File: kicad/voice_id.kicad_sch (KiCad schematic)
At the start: 23 parts, among them J1 Conn_01x08, J2 Audio Out (Speaker), J3 Reset, J4 Fan (5V 0.1A), J6 RV 10k, J7 Conn_01x04, SW1 PWR_SW, U2 LM7805_TO220, U3 Pico

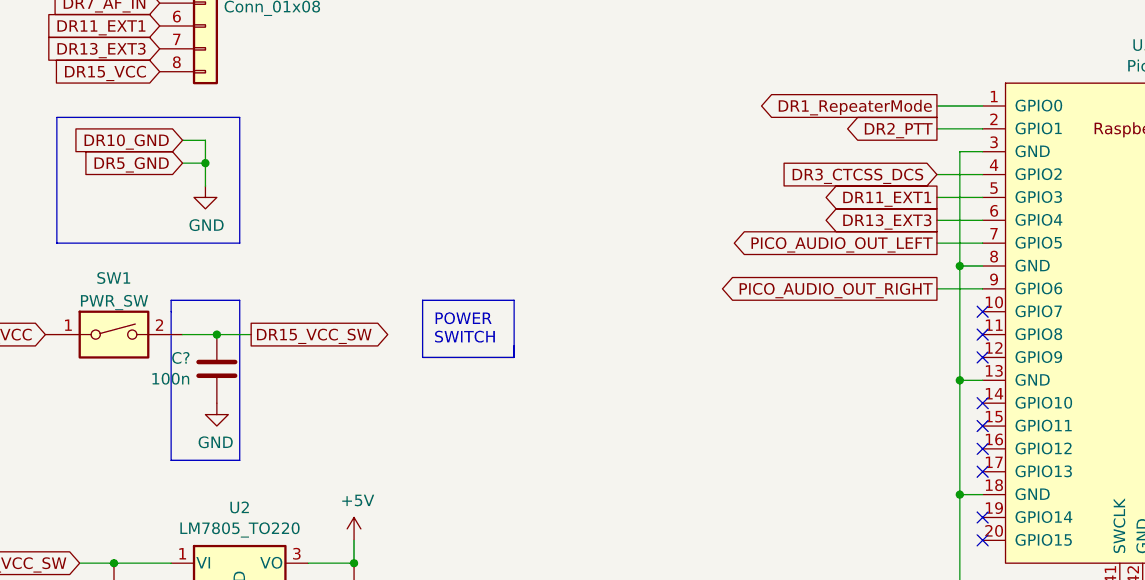
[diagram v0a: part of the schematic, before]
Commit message: Added 100n capacitor to ctcss pin (c9)
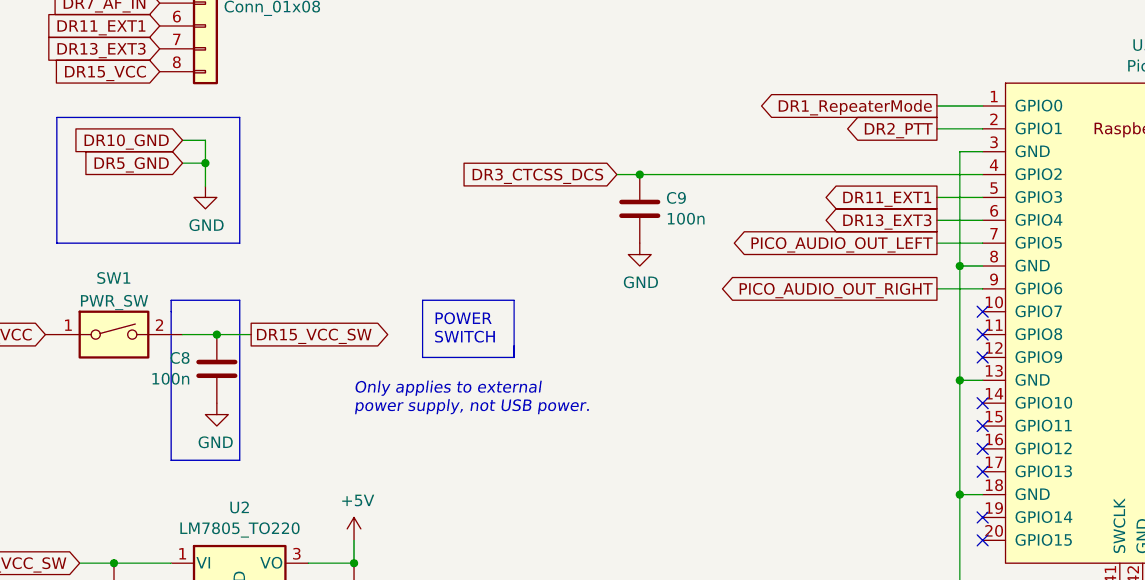
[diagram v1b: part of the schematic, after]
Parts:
- added C9: 100n, Capacitor_THT:C_Disc_D5.0mm_W2.5mm_P5.00mm, symbol Device:C
- gave numbers to parts that had none: 1
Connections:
- net DR3_CTCSS_DCS: now also C9.1
- net GND: now also C9.2
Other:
- note added: "Only applies to external power supply, not USB power."
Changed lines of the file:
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@@
     (title "PicoIDx")
     (date "2021-12-28")
-    (rev "1.0")
+    (rev "1.1")
     (company "#pragma | CT1ENQ")
     (comment 2 "Raspberry Pi Pico  YAESU DR-x Repeater Voice ID Project")
@@
   )
   (junction (at 53.34 119.38) (diameter 0) (color 0 0 0 0)
+  )
+  (junction (at 104.14 53.34) (diameter 0) (color 0 0 0 0)
   )
   (junction (at 90.17 123.19) (diameter 0) (color 0 0 0 0)
@@
     (stroke (width 0) (type default) (color 0 0 0 0))
   )
-  (wire (pts (xy 137.16 53.34) (xy 142.24 53.34))
+  (wire (pts (xy 104.14 53.34) (xy 142.24 53.34))
     (stroke (width 0) (type default) (color 0 0 0 0))
   )
@@
   )
   (wire (pts (xy 203.2 147.32) (xy 204.47 147.32))
+    (stroke (width 0) (type default) (color 0 0 0 0))
+  )
+  (wire (pts (xy 101.6 53.34) (xy 104.14 53.34))
     (stroke (width 0) (type default) (color 0 0 0 0))
   )
@@
     (effects (font (size 1.27 1.27)) (justify left bottom))
   )
+  (text "Only applies to external\npower supply, not USB power."
+    (at 72.39 80.01 0)
+    (effects (font (size 1.27 1.27) italic) (justify left bottom))
+  )
   (text "LED OUTPUTS\n\n1 - D1 - LED POWER ON\n2 - D2 - LED ID ACTIVE\n3 - D3 - LED RX CTCSS"
     (at 238.76 154.94 0)
@@
     )
   )
-  (global_label "DR3_CTCSS_DCS" (shape input) (at 137.16 53.34 180) (fields_autoplaced)
-    (effects (font (size 1.27 1.27)) (justify right))
-    (property "Intersheet References" "${INTERSHEET_REFS}" (id 0) (at 119.4748 53.2606 0)
+  (global_label "DR3_CTCSS_DCS" (shape input) (at 101.6 53.34 180) (fields_autoplaced)
+    (effects (font (size 1.27 1.27)) (justify right))
+    (property "Intersheet References" "${INTERSHEET_REFS}" (id 0) (at 83.9148 53.2606 0)
       (effects (font (size 1.27 1.27)) (justify right) hide)
     )
@@
     (pin "2")
   )
+  (symbol (lib_id "power:GND") (at 104.14 60.96 0) (unit 1)
+    (in_bom yes) (on_board yes)
+    (property "Reference" "#PWR09" (id 0) (at 104.14 67.31 0)
+      (effects (font (size 1.27 1.27)) hide)
+    )
+    (property "Value" "GND" (id 1) (at 104.267 65.3542 0))
+    (property "Footprint" "" (id 2) (at 104.14 60.96 0)
+      (effects (font (size 1.27 1.27)) hide)
+    )
+    (property "Datasheet" "" (id 3) (at 104.14 60.96 0)
+      (effects (font (size 1.27 1.27)) hide)
+    )
+    (pin "1")
+  )
   (symbol (lib_id "Connector_Generic:Conn_01x04") (at 53.34 142.24 0) (unit 1)
     (in_bom yes) (on_board yes) (fields_autoplaced)
@@
     )
     (pin "1")
+  )
+  (symbol (lib_id "Device:C") (at 104.14 57.15 0) (unit 1)
+    (in_bom yes) (on_board yes)
+    (property "Reference" "C9" (id 0) (at 107.061 55.9816 0)
+      (effects (font (size 1.27 1.27)) (justify left))
+    )
+    (property "Value" "100n" (id 1) (at 107.061 58.293 0)
+      (effects (font (size 1.27 1.27)) (justify left))
+    )
+    (property "Footprint" "Capacitor_THT:C_Disc_D5.0mm_W2.5mm_P5.00mm" (id 2) (at 105.1052 60.96 0)
+      (effects (font (size 1.27 1.27)) hide)
+    )
+    (property "Datasheet" "~" (id 3) (at 104.14 57.15 0)
+      (effects (font (size 1.27 1.27)) hide)
+    )
+    (pin "1")
+    (pin "2")
   )
   (symbol (lib_id "power:GND") (at 262.89 86.36 0) (mirror y) (unit 1)
@@
   (symbol (lib_id "Device:C") (at 57.15 74.93 0) (mirror y) (unit 1)
     (in_bom yes) (on_board yes)
-    (property "Reference" "C?" (id 0) (at 54.229 73.7616 0)
+    (property "Reference" "C8" (id 0) (at 54.229 73.7616 0)
       (effects (font (size 1.27 1.27)) (justify left))
     )
@@
   (symbol (lib_id "power:GND") (at 57.15 78.74 0) (mirror y) (unit 1)
     (in_bom yes) (on_board yes)
-    (property "Reference" "#PWR?" (id 0) (at 57.15 85.09 0)
+    (property "Reference" "#PWR08" (id 0) (at 57.15 85.09 0)
       (effects (font (size 1.27 1.27)) hide)
     )
@@
       (reference "#PWR07") (unit 1) (value "GND") (footprint "")
     )
+    (path "/eaa8ee98-cb55-4096-a8d9-742e87453827"
+      (reference "#PWR08") (unit 1) (value "GND") (footprint "")
+    )
+    (path "/13832302-0438-4259-849c-25e4e5c966c7"
+      (reference "#PWR09") (unit 1) (value "GND") (footprint "")
+    )
     (path "/00000000-0000-0000-0000-000061cbc093"
       (reference "#PWR0101") (unit 1) (value "+5V") (footprint "")
@@
       (reference "#PWR0116") (unit 1) (value "GND") (footprint "")
     )
-    (path "/eaa8ee98-cb55-4096-a8d9-742e87453827"
-      (reference "#PWR?") (unit 1) (value "GND") (footprint "")
-    )
     (path "/00000000-0000-0000-0000-000061d2f610"
       (reference "C1") (unit 1) (value "0.33u") (footprint "Capacitor_THT:CP_Radial_D5.0mm_P2.50mm")
@@
     )
     (path "/bdb20a4c-bb1a-4359-89d7-91df4459a59b"
-      (reference "C?") (unit 1) (value "100n") (footprint "Capacitor_THT:C_Disc_D5.0mm_W2.5mm_P5.00mm")
+      (reference "C8") (unit 1) (value "100n") (footprint "Capacitor_THT:C_Disc_D5.0mm_W2.5mm_P5.00mm")
+    )
+    (path "/612c4877-8845-42fd-8e80-01cd946c7579"
+      (reference "C9") (unit 1) (value "100n") (footprint "Capacitor_THT:C_Disc_D5.0mm_W2.5mm_P5.00mm")
     )
     (path "/12323070-18ea-482f-8737-97cc868617fb"
